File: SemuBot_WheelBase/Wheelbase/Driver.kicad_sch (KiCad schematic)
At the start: 22 parts, among them Q1 DI025N06PT-AQ, Q2 DI025N06PT-AQ, Q3 DI025N06PT-AQ, Q4 DI025N06PT-AQ, Q5 DI025N06PT-AQ, Q6 DI025N06PT-AQ, U2 DRV8353FSRTAR

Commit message: Random push
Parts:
- removed C4: 4.7uF, Capacitor_SMD:C_0603_1608Metric_Pad1.08x0.95mm_HandSolder, symbol Device:C
- added C28: 1uF, Capacitor_SMD:C_0603_1608Metric_Pad1.08x0.95mm_HandSolder, symbol Device:C
- added C31: 22uF, Capacitor_SMD:C_0805_2012Metric_Pad1.18x1.45mm_HandSolder, symbol Device:C
- C7: value 0.1uF -> 10uF
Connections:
- net +24V: now also C5.1, U2.3 (VM), C31.2
- net +5V: no longer C5.1, U2.3 (VM)
- net GND: now also C28.1, C31.1
- net at U2.1 (CPL): now also C8.2
- net at U2.40 (VGLS): now also C28.2; no longer C8.2
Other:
- moved on the sheet: C8

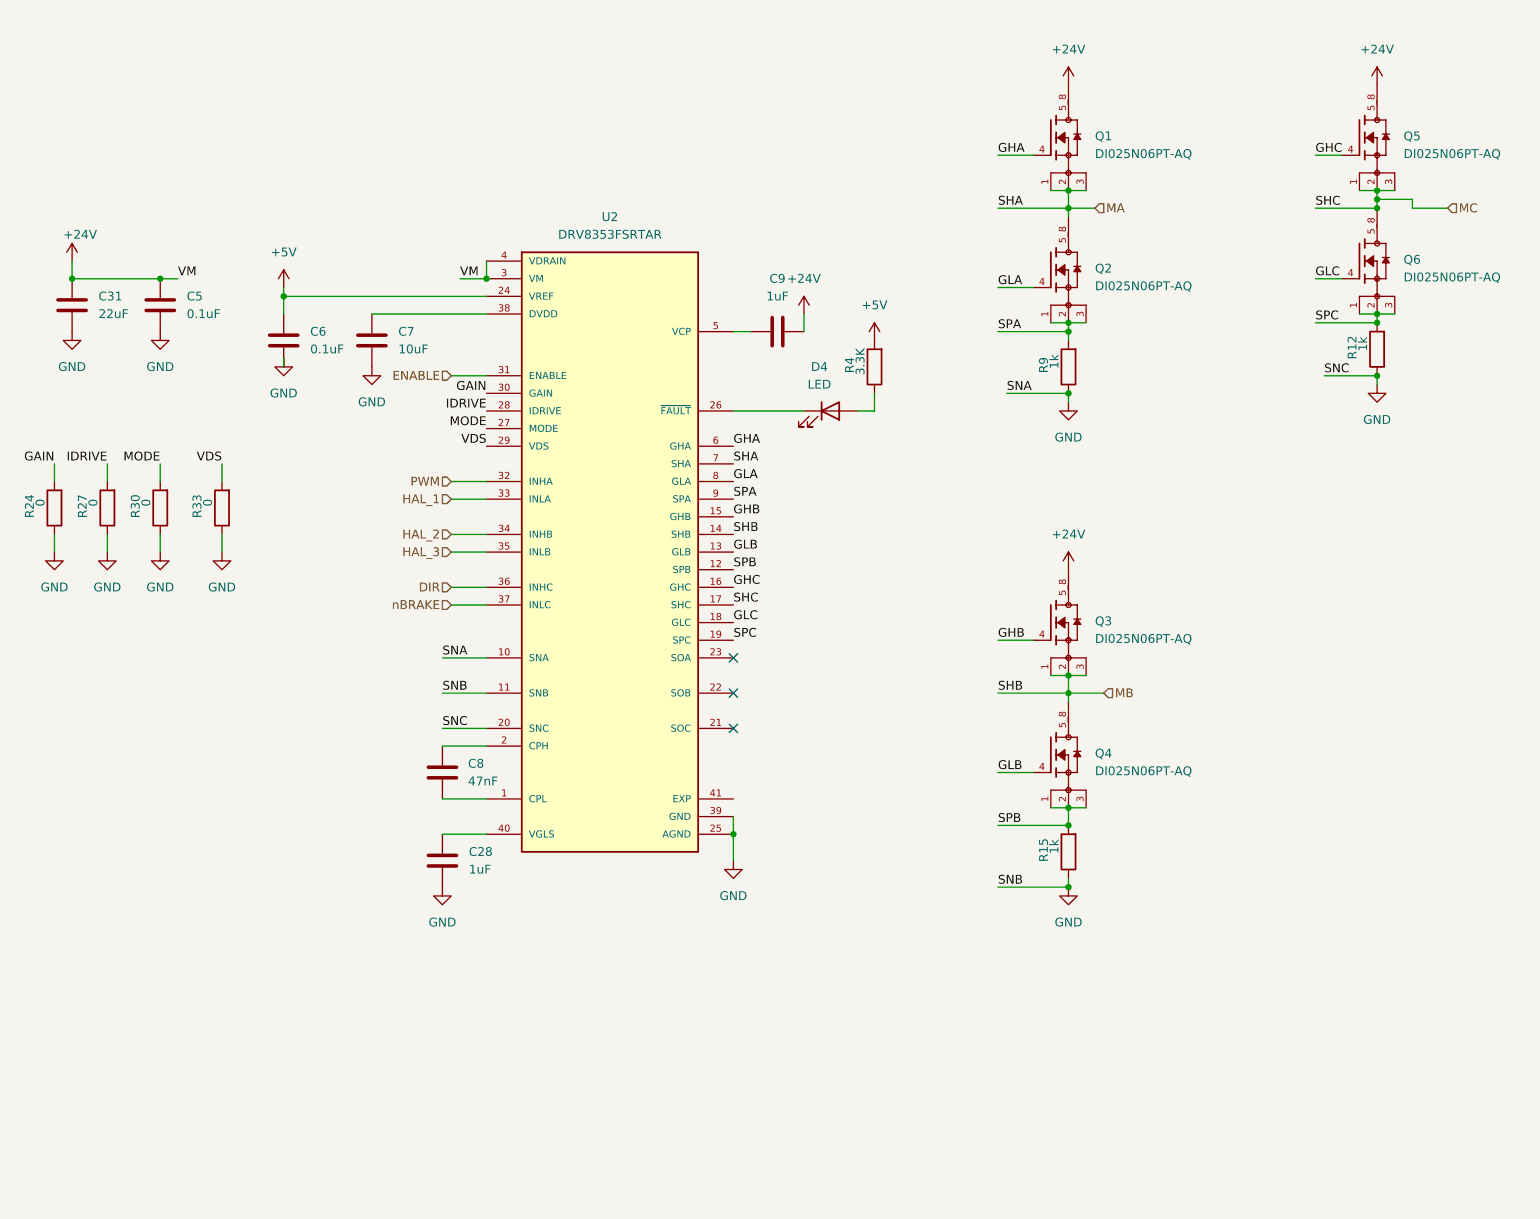
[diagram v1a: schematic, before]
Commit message: Wheelbase HW version and SPI version.
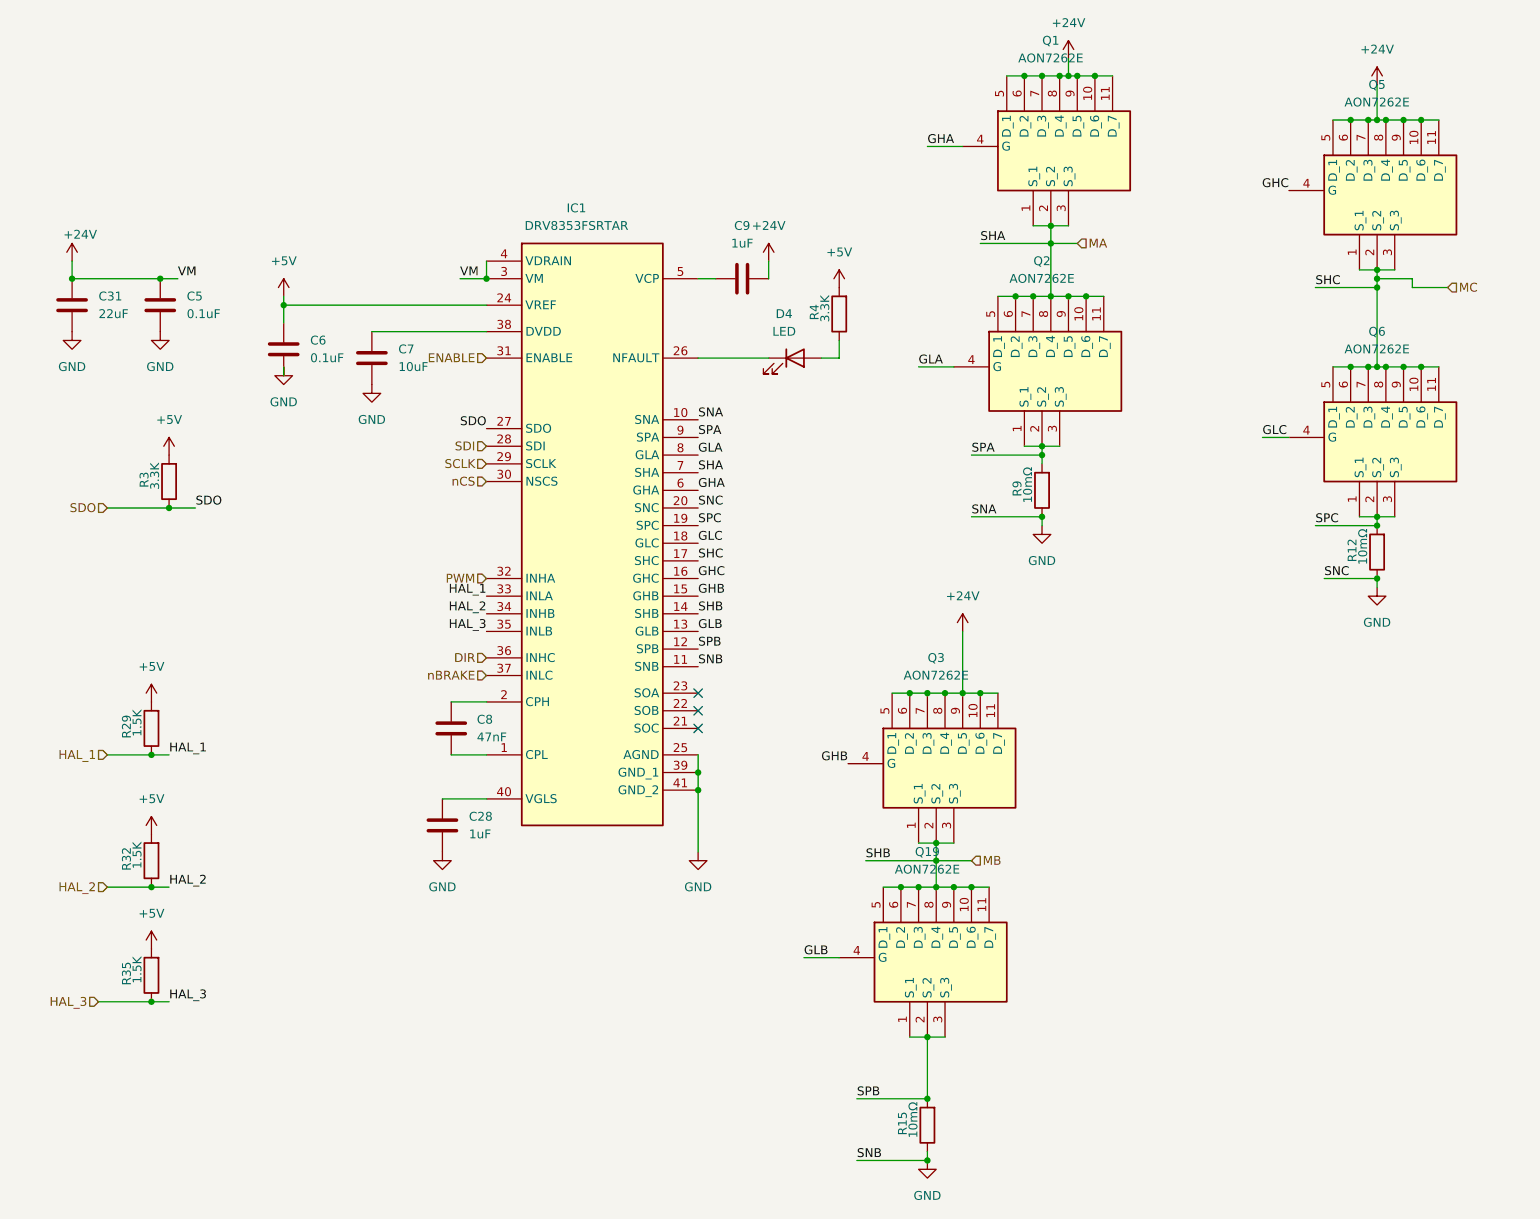
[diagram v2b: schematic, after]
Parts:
- removed Q1, Q2, Q3, Q4, Q5, Q6: DI025N06PT-AQ, DI025N06PT-AQ:TRANS_DI025N06PT-AQ, symbol DI025N06PT-AQ:DI025N06PT-AQ
- removed R24, R27, R30, R33: 0, Resistor_SMD:R_0603_1608Metric_Pad0.98x0.95mm_HandSolder, symbol Device:R
- removed U2: DRV8353FSRTAR, DRV8353HRTAT(1):QFN50P600X600X80-41N, symbol DRV8353HRTAT:DRV8353HRTAT
- added IC1: DRV8353FSRTAR, DRV8358FSTAR:QFN50P600X600X80-41N-D, symbol DRV8353FSRTAR:DRV8353FSRTAR
- added Q1, Q19, Q2, Q3, Q5, Q6: AON7262E, AON7262E, symbol AON7262E:AON7262E
- added R29, R32, R35: 1.5K, Resistor_SMD:R_0603_1608Metric_Pad0.98x0.95mm_HandSolder, symbol Device:R
- added R3: 3.3K, Resistor_SMD:R_0603_1608Metric_Pad0.98x0.95mm_HandSolder, symbol Device:R
- R12, R15, R9: value 1k -> 10mΩ; footprint Resistor_SMD:R_0603_1608Metric_Pad0.98x0.95mm_HandSolder -> Resistor_SMD:R_2512_6332Metric_Pad1.40x3.35mm_HandSolder
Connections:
- net +24V: now also IC1.3 (VM), IC1.4 (VDRAIN), Q1.10 (D_6), Q1.11 (D_7), Q1.5 (D_1), Q1.6 (D_2), Q1.7 (D_3), Q1.8 (D_4), Q1.9 (D_5), Q3.10 (D_6), Q3.11 (D_7), Q3.5 (D_1), Q3.6 (D_2), Q3.7 (D_3), Q3.8 (D_4), Q3.9 (D_5), Q5.10 (D_6), Q5.11 (D_7), Q5.5 (D_1), Q5.6 (D_2), Q5.7 (D_3), Q5.8 (D_4), Q5.9 (D_5)
- net +5V: now also IC1.24 (VREF), R29.2, R3.2, R32.2, R35.2
- net DIR: now also IC1.36 (INHC)
- net ENABLE: now also IC1.31 (ENABLE)
- net GHA: now also IC1.6 (GHA), Q1.4 (G)
- net GHB: now also IC1.15 (GHB), Q3.4 (G)
- net GHC: now also IC1.16 (GHC), Q5.4 (G)
- net GLA: now also IC1.8 (GLA), Q2.4 (G)
- net GLB: now also IC1.13 (GLB), Q19.4 (G)
- net GLC: now also IC1.18 (GLC), Q6.4 (G)
- net GND: now also IC1.10 (SNA), IC1.11 (SNB), IC1.20 (SNC), IC1.25 (AGND), IC1.39 (GND_1), IC1.41 (GND_2)
- net HAL_1: now also IC1.33 (INLA), R29.1
- net HAL_2: now also IC1.34 (INHB), R32.1
- net HAL_3: now also IC1.35 (INLB), R35.1
- net MA: now also IC1.7 (SHA), Q1.1 (S_1), Q1.2 (S_2), Q1.3 (S_3), Q2.10 (D_6), Q2.11 (D_7), Q2.5 (D_1), Q2.6 (D_2), Q2.7 (D_3), Q2.8 (D_4), Q2.9 (D_5)
- net MB: now also IC1.14 (SHB), Q19.10 (D_6), Q19.11 (D_7), Q19.5 (D_1), Q19.6 (D_2), Q19.7 (D_3), Q19.8 (D_4), Q19.9 (D_5), Q3.1 (S_1), Q3.2 (S_2), Q3.3 (S_3)
- net MC: now also IC1.17 (SHC), Q5.1 (S_1), Q5.2 (S_2), Q5.3 (S_3), Q6.10 (D_6), Q6.11 (D_7), Q6.5 (D_1), Q6.6 (D_2), Q6.7 (D_3), Q6.8 (D_4), Q6.9 (D_5)
- net PWM: now also IC1.32 (INHA)
- net SPA: now also IC1.9 (SPA), Q2.1 (S_1), Q2.2 (S_2), Q2.3 (S_3)
- net SPB: now also IC1.12 (SPB), Q19.1 (S_1), Q19.2 (S_2), Q19.3 (S_3)
- net SPC: now also IC1.19 (SPC), Q6.1 (S_1), Q6.2 (S_2), Q6.3 (S_3)
- net nBRAKE: now also IC1.37 (INLC)
- net at C7.1: now also IC1.38 (DVDD)
- net at D4.1 (K): now also IC1.26 (NFAULT)
- net at C9.1: now also IC1.5 (VCP)
- net at C8.2: now also IC1.1 (CPL)
- net at C8.1: now also IC1.2 (CPH)
- net at C28.2: now also IC1.40 (VGLS)
- new net SCLK: IC1.29 (SCLK)
- new net SDI: IC1.28 (SDI)
- new net SDO: IC1.27 (SDO), R3.1
- new net nCS: IC1.30 (NSCS)
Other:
- moved on the sheet: C28, C6, C7, C8, C9, D4, R12, R15, R4, R9
